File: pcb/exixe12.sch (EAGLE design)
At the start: 42 parts

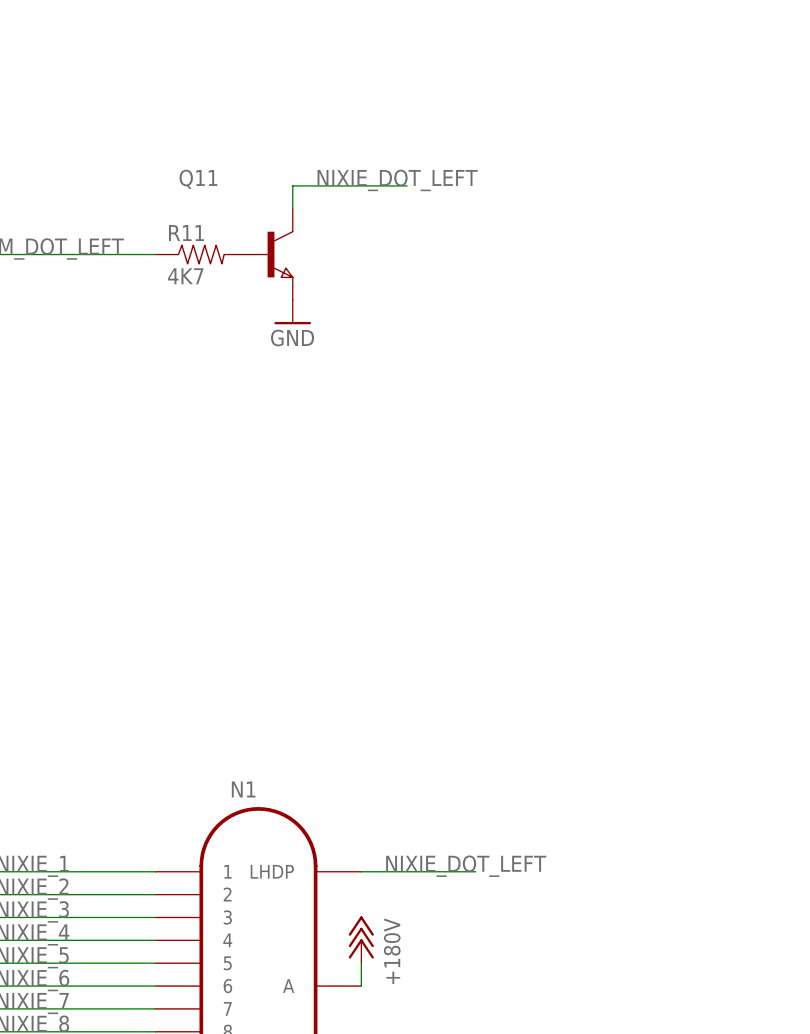
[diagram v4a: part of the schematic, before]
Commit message: added nixie dot current limit resistor
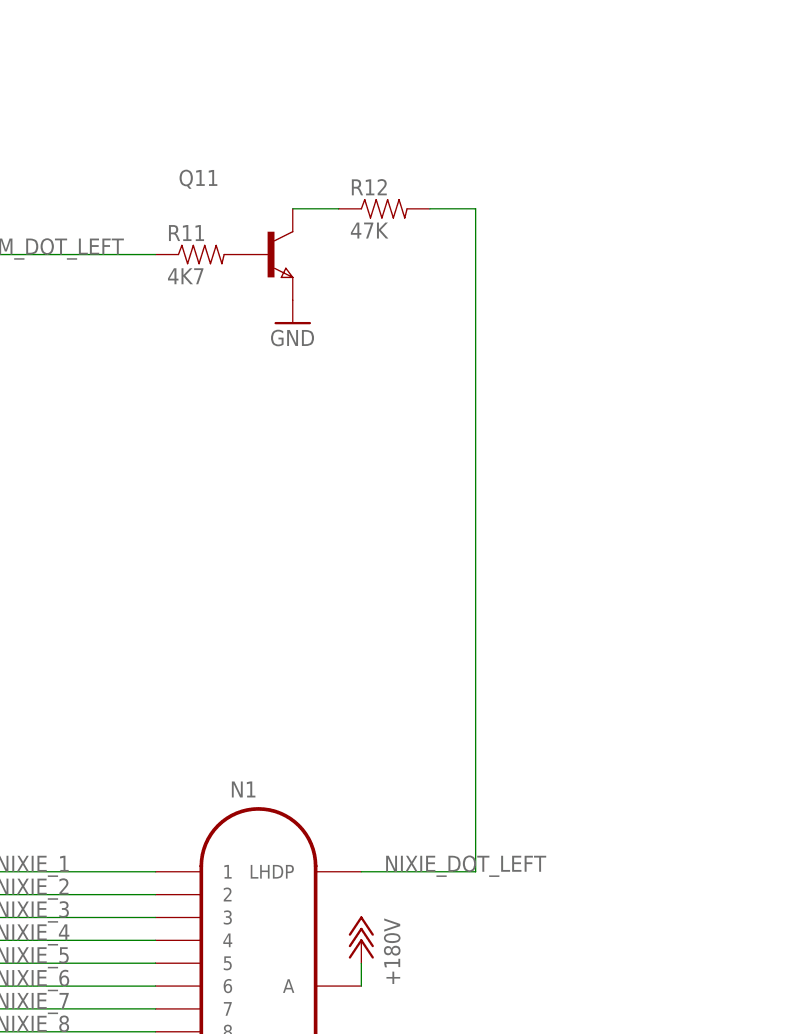
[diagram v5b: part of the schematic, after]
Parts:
- added R12: 47K, joyAnalog:RESISTOR0805-RES
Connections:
- new net N$22: Q11.C, R12.1
- net NIXIE_DOT_LEFT: now also R12.2; no longer Q11.C
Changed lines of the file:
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@@
 <part name="TP5" library="nixx" deviceset="PTR1" device="TP13R"/>
 <part name="TP6" library="nixx" deviceset="PTR1" device="TP13R"/>
+<part name="R12" library="joyAnalog" deviceset="RESISTOR" device="0805-RES" value="47K"/>
 </parts>
 <sheets>
@@
 <instance part="TP5" gate="G$1" x="462.28" y="50.8" rot="R90"/>
 <instance part="TP6" gate="G$1" x="449.58" y="91.44" rot="R90"/>
+<instance part="R12" gate="G$1" x="238.76" y="53.34"/>
 </instances>
 <busses>
@@
 <net name="NIXIE_DOT_LEFT" class="0">
 <segment>
-<pinref part="Q11" gate="A" pin="C"/>
-<wire x1="228.6" y1="53.34" x2="228.6" y2="55.88" width="0.1524" layer="91"/>
-<wire x1="228.6" y1="55.88" x2="241.3" y2="55.88" width="0.1524" layer="91"/>
-<label x="231.14" y="55.88" size="1.778" layer="95"/>
-</segment>
-<segment>
 <wire x1="236.22" y1="-20.32" x2="248.92" y2="-20.32" width="0.1524" layer="91"/>
 <label x="238.76" y="-20.32" size="1.778" layer="95"/>
 <pinref part="N1" gate="G$1" pin="LHDP"/>
+<pinref part="R12" gate="G$1" pin="2"/>
+<wire x1="243.84" y1="53.34" x2="248.92" y2="53.34" width="0.1524" layer="91"/>
+<wire x1="248.92" y1="53.34" x2="248.92" y2="-20.32" width="0.1524" layer="91"/>
 </segment>
 </net>
@@
 </segment>
 </net>
+<net name="N$22" class="0">
+<segment>
+<pinref part="Q11" gate="A" pin="C"/>
+<pinref part="R12" gate="G$1" pin="1"/>
+<wire x1="228.6" y1="53.34" x2="233.68" y2="53.34" width="0.1524" layer="91"/>
+</segment>
+</net>

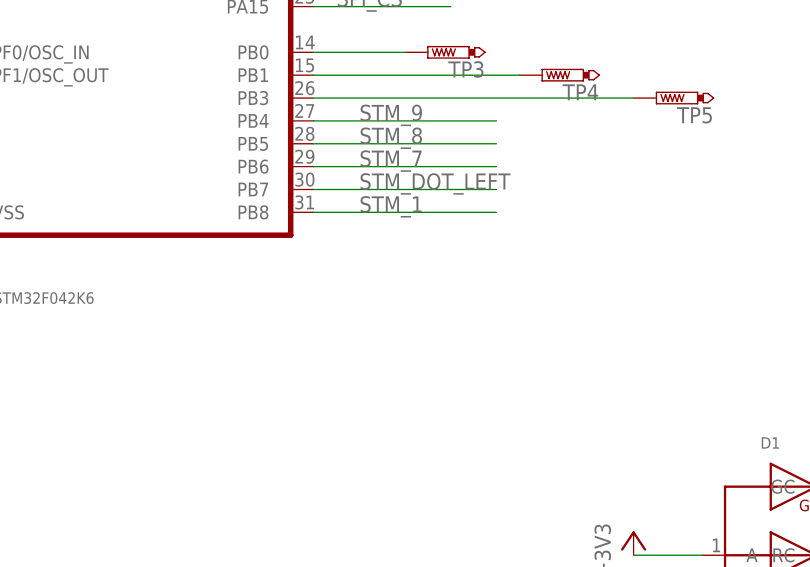
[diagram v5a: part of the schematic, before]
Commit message: added pulldown on boot0
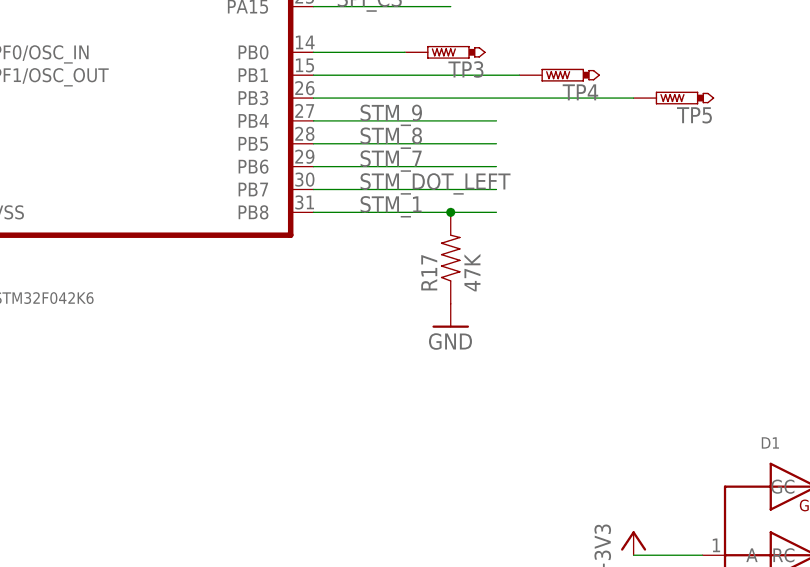
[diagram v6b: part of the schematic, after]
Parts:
- added R17: 47K, joyAnalog:RESISTOR0805-RES
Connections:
- net GND: now also R17.1
- net STM_1: now also R17.2
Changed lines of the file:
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@@
 <part name="TP6" library="nixx" deviceset="PTR1" device="TP13R"/>
 <part name="R12" library="joyAnalog" deviceset="RESISTOR" device="0805-RES" value="47K"/>
+<part name="R17" library="joyAnalog" deviceset="RESISTOR" device="0805-RES" value="47K"/>
+<part name="GND12" library="joyAnalog" deviceset="GND" device=""/>
 </parts>
 <sheets>
@@
 <instance part="TP6" gate="G$1" x="449.58" y="91.44" rot="R90"/>
 <instance part="R12" gate="G$1" x="238.76" y="53.34"/>
+<instance part="R17" gate="G$1" x="439.42" y="33.02" rot="R90"/>
+<instance part="GND12" gate="1" x="439.42" y="25.4"/>
 </instances>
 <busses>
@@
 <wire x1="431.8" y1="-43.18" x2="441.96" y2="-43.18" width="0.1524" layer="91"/>
 </segment>
+<segment>
+<pinref part="R17" gate="G$1" pin="1"/>
+<pinref part="GND12" gate="1" pin="GND"/>
+</segment>
 </net>
 <net name="N$1" class="0">
@@
 <segment>
 <pinref part="U$2" gate="G$1" pin="PB8"/>
-<wire x1="444.5" y1="38.1" x2="424.18" y2="38.1" width="0.1524" layer="91"/>
+<wire x1="444.5" y1="38.1" x2="439.42" y2="38.1" width="0.1524" layer="91"/>
 <label x="429.26" y="38.1" size="1.778" layer="95"/>
-</segment>
-</net>
+<pinref part="R17" gate="G$1" pin="2"/>
+<wire x1="439.42" y1="38.1" x2="424.18" y2="38.1" width="0.1524" layer="91"/>
+<junction x="439.42" y="38.1"/>
+</segment>
+</net>

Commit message: updated to use timer
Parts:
- removed TP4, TP6: PTR1TP13R, nixx:PTR1TP13R
- R1, R10, R11, R18, R2, R3, R4, R5, R6, R7, R8, R9: value 4K7 -> 10K
- R12: value 47K -> 510K
- R15: value 470 -> 1K
- R16: value 0 -> 470
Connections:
- removed net N$18: TP4.TP, U$2.PB1
- removed net N$20: TP5.TP, U$2.PB3
- net N$14: now also TP2.TP, U$2.PB6; no longer TP6.TP, U$2.PA4
- net N$16: now also TP3.TP, U$2.PF0/OSC_IN; no longer TP2.TP, U$2.PA10
- net N$17: now also TP5.TP, U$2.PF1/OSC_OUT; no longer TP3.TP, U$2.PB0
- net PWM_BLUE: now also U$2.PA10; no longer U$2.PA11
- net STM_10: now also U$2.PA11; no longer U$2.PA12
- net STM_2: now also U$2.PB0; no longer U$2.PF1/OSC_OUT
- net STM_4: now also U$2.PB1; no longer U$2.PF0/OSC_IN
- net STM_5: now also U$2.PA4
- net STM_7: now also U$2.PB5; no longer U$2.PB6
- net STM_8: now also U$2.PB4; no longer U$2.PB5
- net STM_9: now also U$2.PB3; no longer U$2.PB4
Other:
- moved on the sheet: TP2, TP3, TP5
